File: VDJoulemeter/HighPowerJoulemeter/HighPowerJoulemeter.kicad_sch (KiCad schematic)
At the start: 27 parts, among them J1 XT60-M, J2 XT60-M, U2 TMCS1107A1BQDR, U3 MCP2551-E/P, U4 MIC5219-5.0YM5-TR, U5 MCP6286T-E/OT, U6 PTPSM365R6FRDN, U7 P65630SVCGR, U8 ADS1118QDGSRQ1, U9 MIC5219-3.3YM5-TR

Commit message: fixes from Edwin/Patrick/Solamon feedback
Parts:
- added C15: 0.1uF, symbol Device:C
- added J3, J4: 22035035, SMV_Connectors:3pin_CON_22035035_MOL, symbol SMV_Custom:3-pin Mini Molex Spox
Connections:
- net STM32_GND is gone; now on net GND: U2.5 (GND)
- net 48V_OUT: now also C15.2
- net GND: now also C15.1, J3.2, J4.2
- net CAN_L: now reaches U3.6
- net CAN_L: now also J3.3, J4.3
- net CAN_H: now reaches U3.7
- net CAN_H: now also J3.1, J4.1
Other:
- note removed: "CAN Connector Pin 2 (GND) connects to the same logic ground as the VSS Pin"
- moved on the sheet: C6

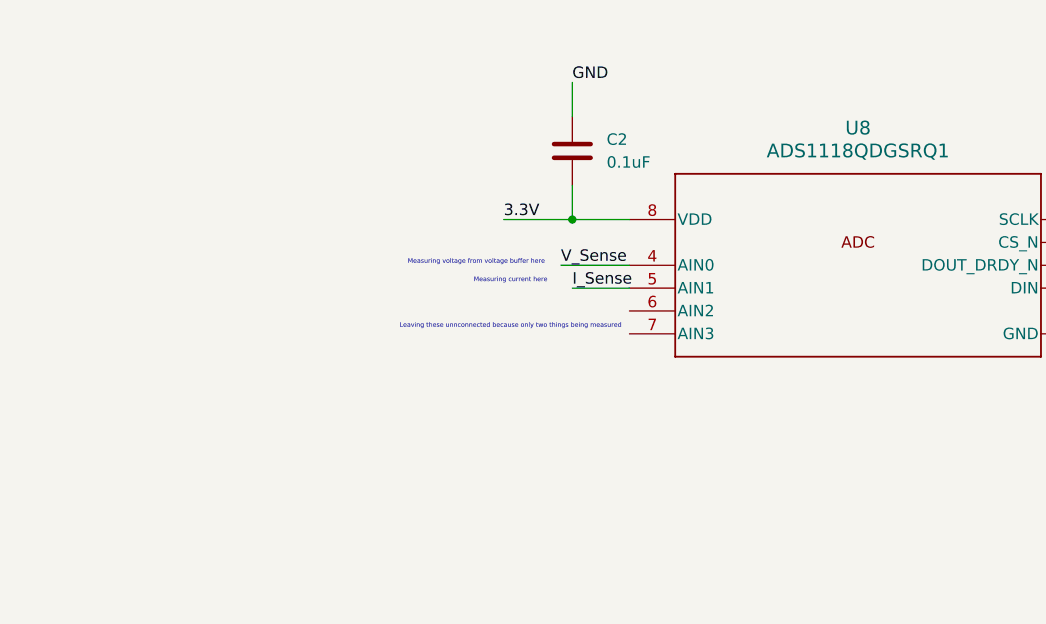
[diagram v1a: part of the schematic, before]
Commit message: added RC filters for ADC inputs
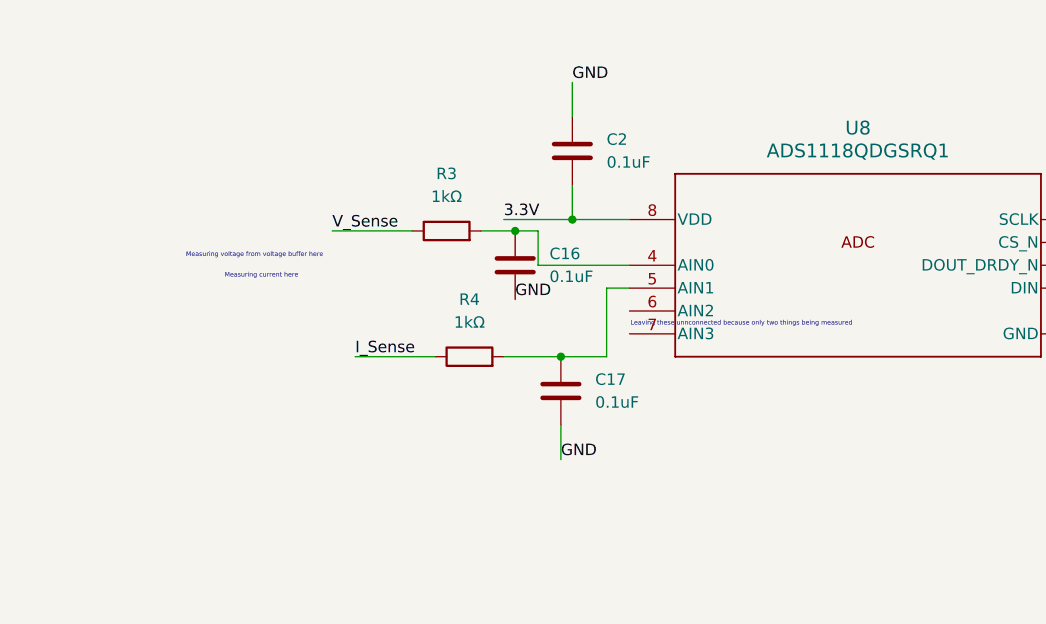
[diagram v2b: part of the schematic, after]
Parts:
- added C16, C17: 0.1uF, symbol Device:C
- added R3, R4: 1kΩ, symbol Device:R
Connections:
- net GND: now also C16.2, C17.2
- net I_Sense: now also R4.1; no longer U8.5 (AIN1)
- net V_Sense: now also R3.1; no longer U8.4 (AIN0)
- new net: C16.1, R3.2, U8.4 (AIN0)
- new net: C17.1, R4.2, U8.5 (AIN1)

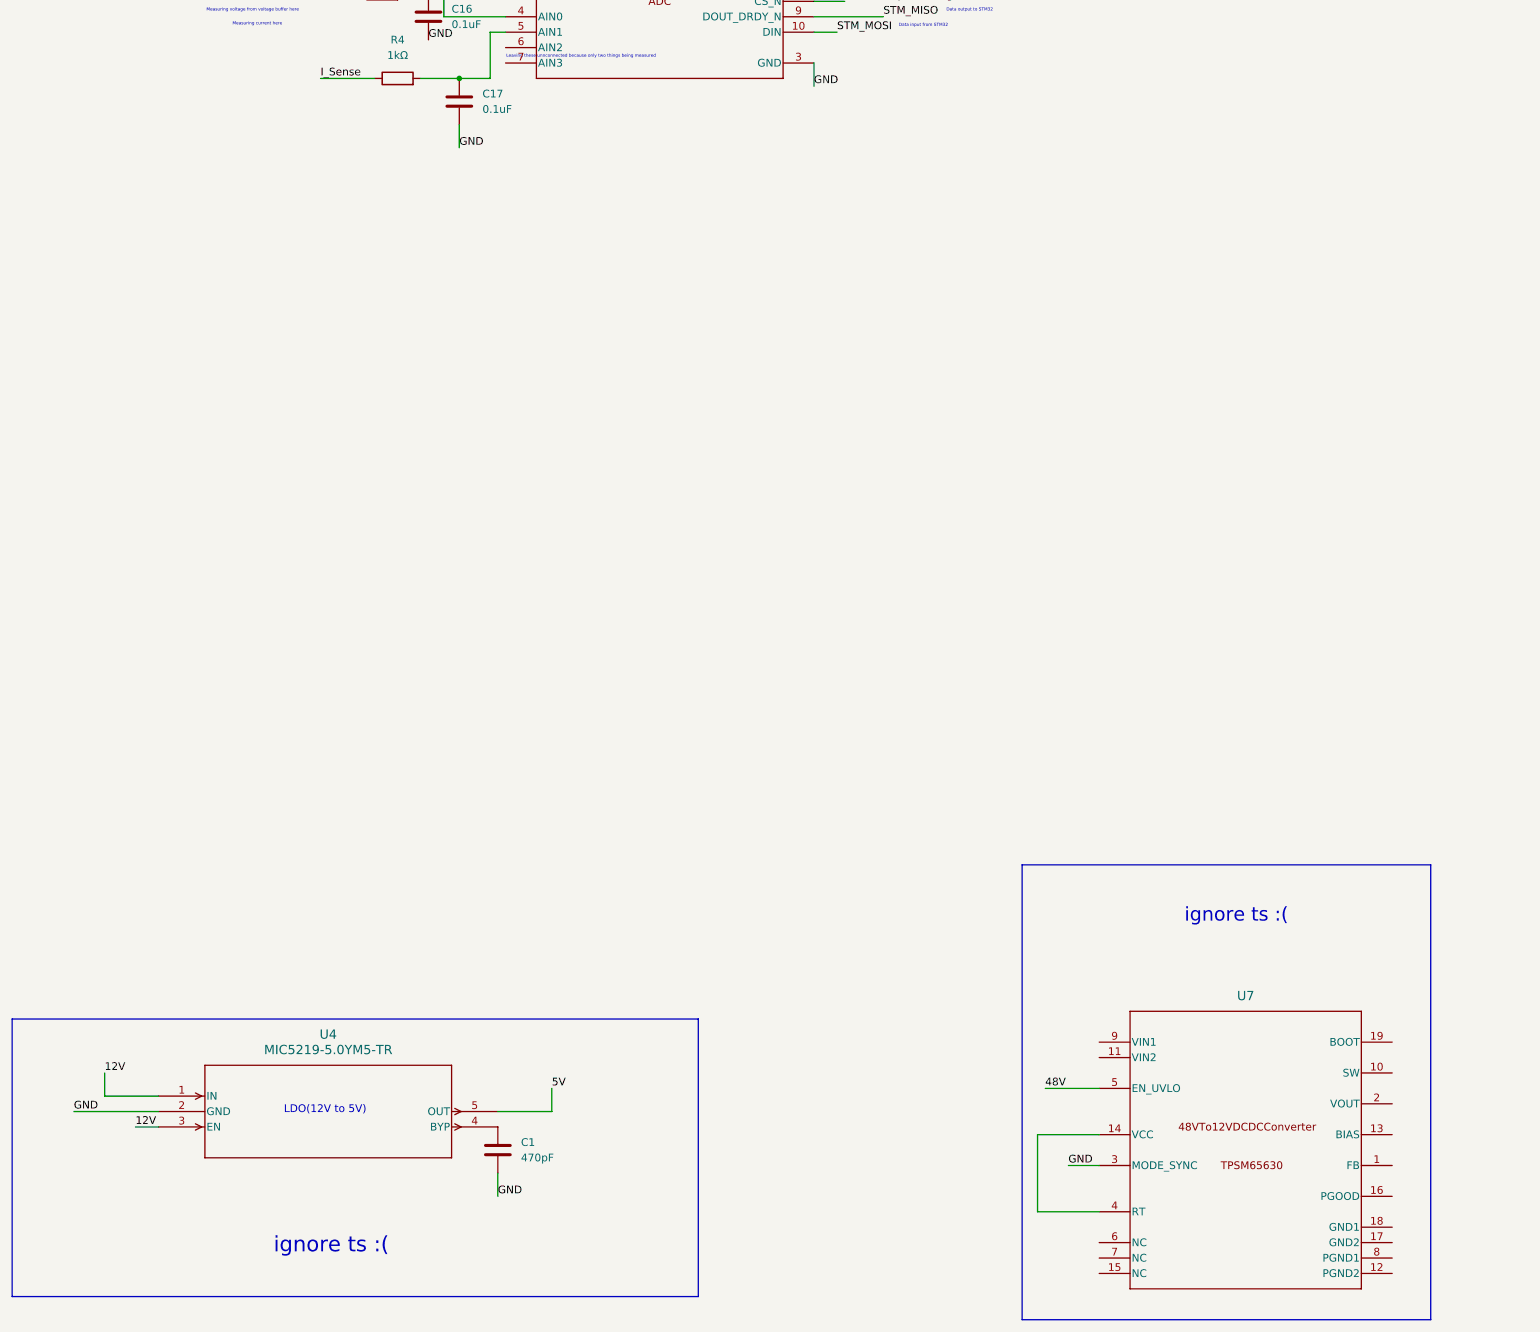
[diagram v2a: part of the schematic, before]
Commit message: still need to add test pads and power symbols
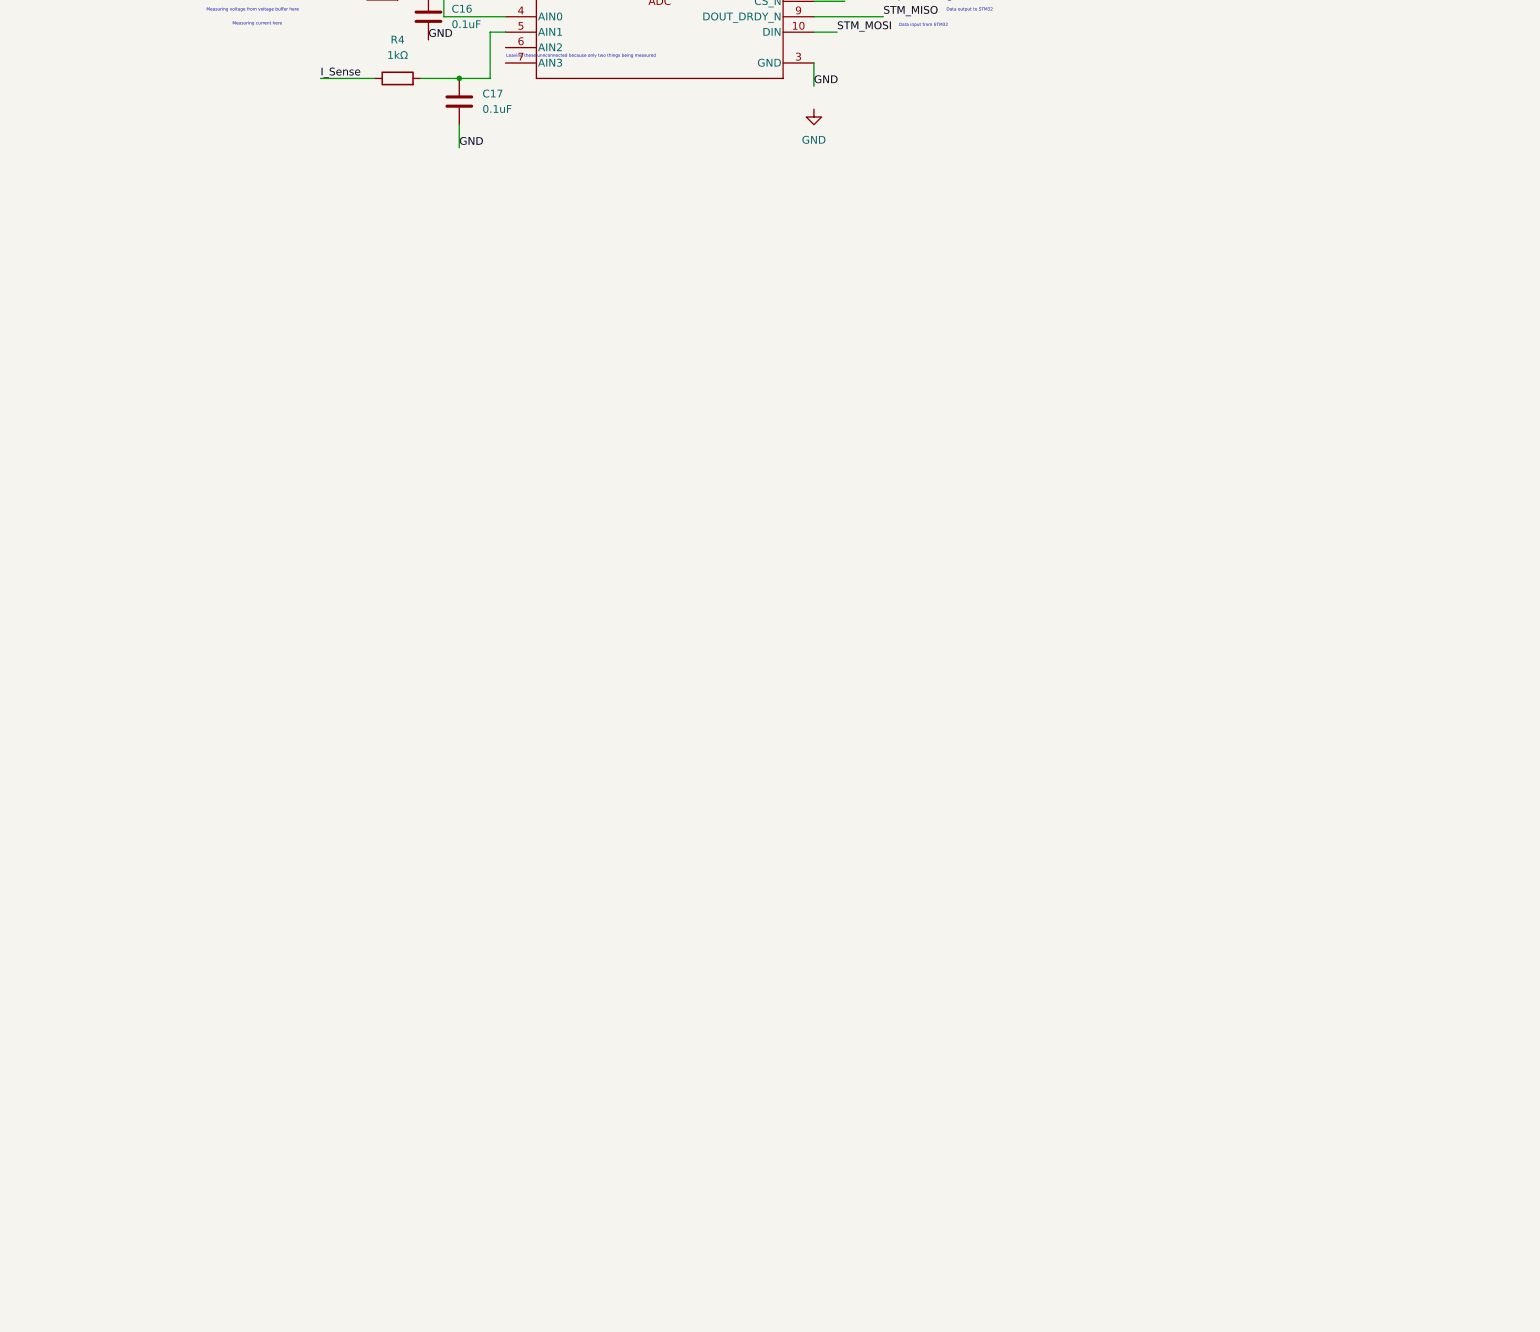
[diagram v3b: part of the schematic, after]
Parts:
- removed C1: 470pF, symbol Device:C
- removed U4: MIC5219-5.0YM5-TR, SOT-23-5_M5_MCH, symbol SMV_Custom:MIC5219-5.0YM5-TR
- removed U7: P65630SVCGR, VCG0019A-MFG, symbol SMV_Custom:P65630SVCGR
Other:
- note removed: "LDO(12V to 5V)"
- note removed: "ignore ts :("

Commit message: added symbols
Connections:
- net 5V: no longer C5.1, C8.1, C9.1, U3.3, U6.4 (VOUT), U6.9 (BIAS), U9.3 (EN)
- net 3.3V renamed +3.3V
- new net +5V: C5.1, C8.1, C9.1, U3.3, U6.4 (VOUT), U6.9 (BIAS), U9.3 (EN)
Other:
- moved on the sheet: C5, J3

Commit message: added some test pads
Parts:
- added TP1, TP2, TP3, TP4, TP5, TP6, TP7: TestPoint, symbol Connector:TestPoint
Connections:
- net 5V is gone; now on net +5V: U9.1 (IN)
- net +3.3V: now also TP7.1
- net +5V: now also TP5.1, TP6.1
- net 48V_IN: now also TP2.1
- net 48V_OUT: now also TP3.1, TP4.1
- net VoltageDividerOut: now also TP1.1
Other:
- moved on the sheet: C10, J2, R1, R2

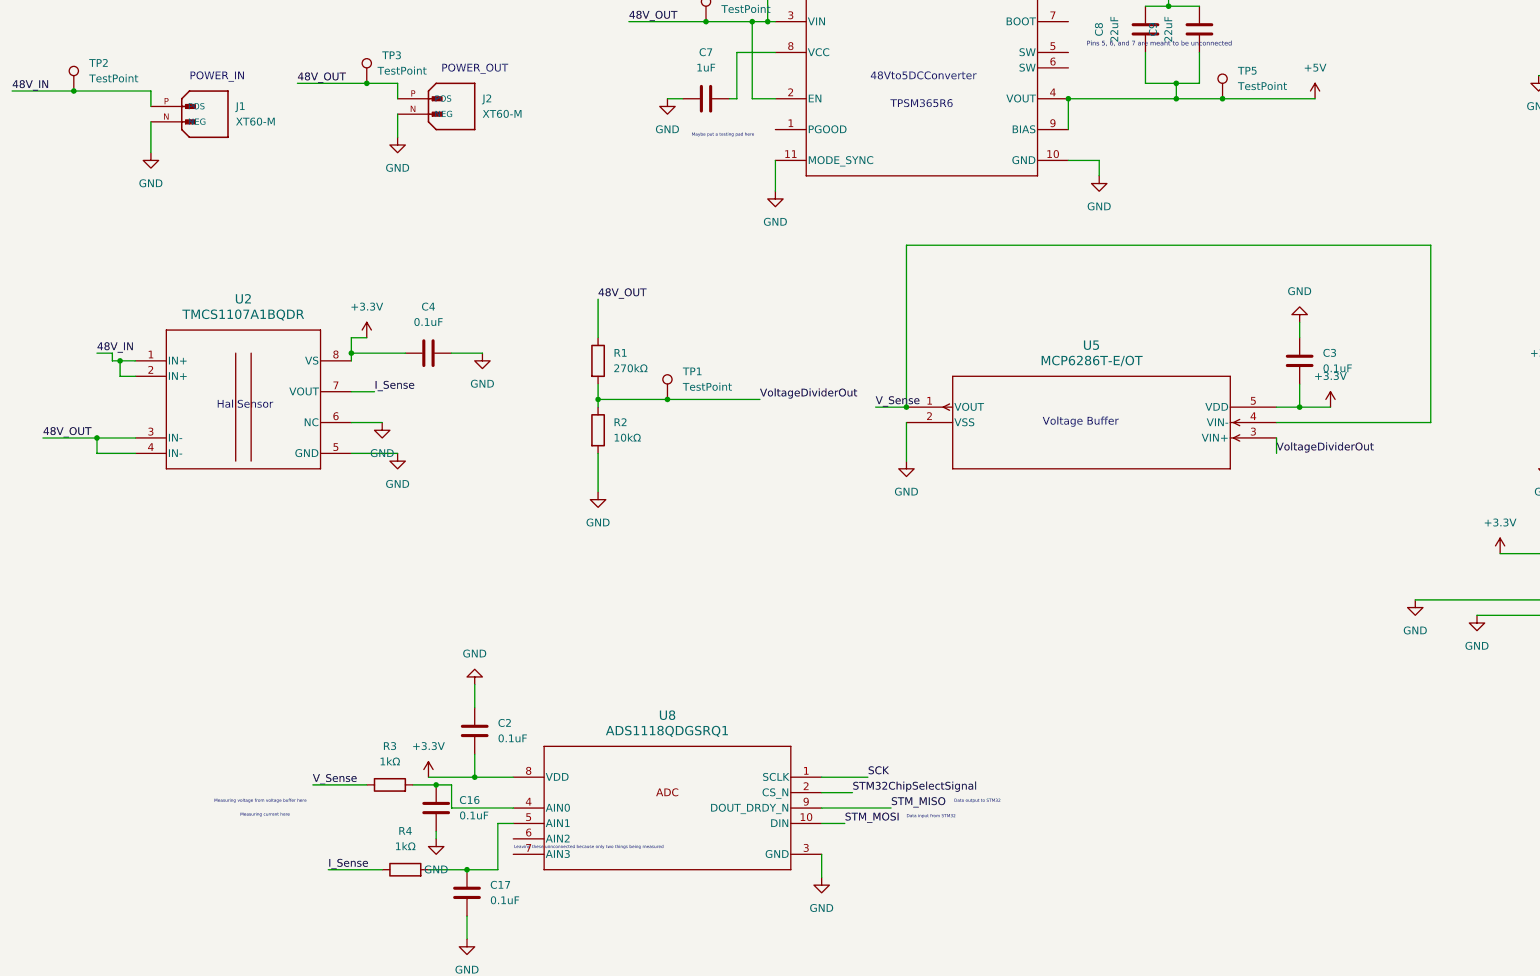
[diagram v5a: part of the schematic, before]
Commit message: Added and labeled multiple test pads
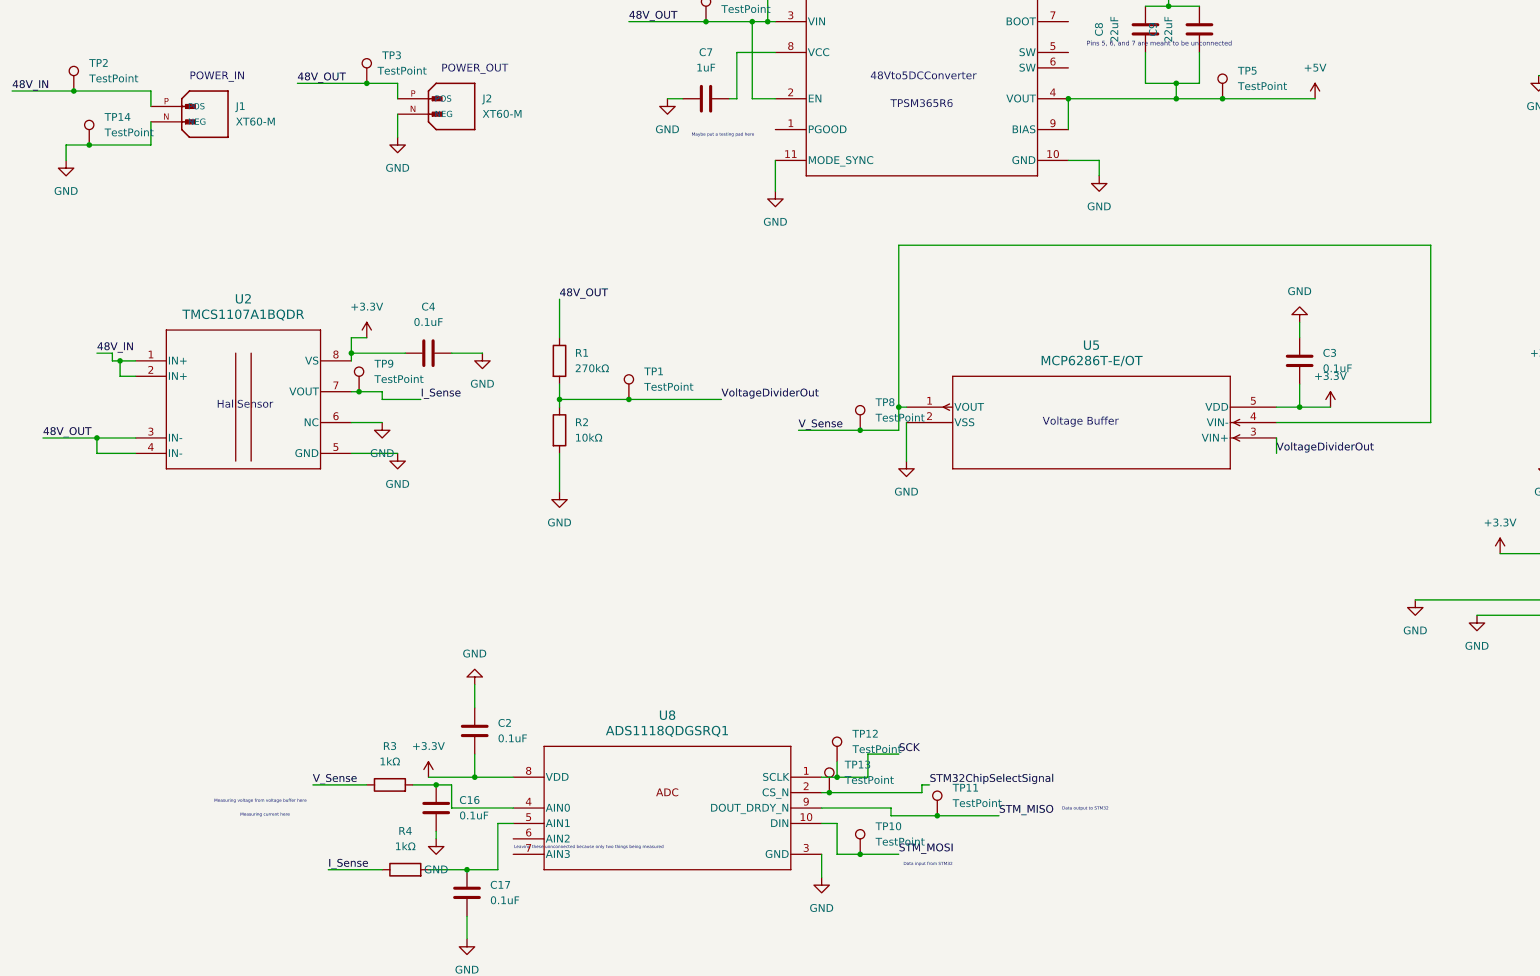
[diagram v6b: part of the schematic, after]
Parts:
- added TP10, TP11, TP12, TP13, TP14, TP8, TP9: TestPoint, symbol Connector:TestPoint
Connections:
- net GND: now also TP14.1
- net I_Sense: now also TP9.1
- net SCK: now also TP12.1
- net STM32ChipSelectSignal: now also TP13.1
- net STM_MISO: now also TP11.1
- net STM_MOSI: now also TP10.1
- net V_Sense: now also TP8.1
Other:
- moved on the sheet: R1, R2, TP1
